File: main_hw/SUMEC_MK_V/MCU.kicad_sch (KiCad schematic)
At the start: 3 parts, among them U2 ESP32-S3-WROOM-1

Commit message: MK V Schematic update
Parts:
- added C34: 100n, Capacitor_SMD:C_0402_1005Metric, symbol Device:C
- added C35: 100nF, Capacitor_SMD:C_0805_2012Metric_Pad1.18x1.45mm_HandSolder, symbol Device:C
- added EEPROM1: 24CW1280T-I_OT, 24CW1280T-I_OT:SOT95P280X145-5N, symbol 24CW1280T-I_OT:24CW1280T-I_OT
- added U8: 24CW1280T-I/OT, Package_TO_SOT_SMD:SOT-23-5, symbol Memory_EEPROM:24AA02-OT
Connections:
- net +3V3: now also C34.1, C35.1, EEPROM1.4 (VCC), U8.4 (V_{CC})
- net GND: now also C34.2, C35.2, EEPROM1.2 (VSS), U8.2 (V_{SS})
- net SCL: now also U8.1 (SCL)
- net SDA: now also U8.3 (SDA)
- new net I2C1_SCL: EEPROM1.1 (SCL)
- new net I2C1_SDA: EEPROM1.3 (SDA)
- no-connect marks 5 -> 7
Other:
- note added: "CHANGE LABELS"
- note added: "EEPROM"
- note added: "I2C Addr.: 0x50"
- moved on the sheet: C20, C21, U2

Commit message: Schematic update - finalized
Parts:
- removed C34: 100n, Capacitor_SMD:C_0402_1005Metric, symbol Device:C
- removed EEPROM1: 24CW1280T-I_OT, 24CW1280T-I_OT:SOT95P280X145-5N, symbol 24CW1280T-I_OT:24CW1280T-I_OT
- removed U2: ESP32-S3-WROOM-1, PCM_Espressif:ESP32-S3-WROOM-1, symbol sumec_sch_lib:ESP32-S3-WROOM-1_CUSTOM_made_by_bismarx
- added U4: ESP32-S3-WROOM-1, PCM_Espressif:ESP32-S3-WROOM-1, symbol sumec_sch_lib:ESP32-S3-WROOM-1_CUSTOM_made_by_bismarx
- renumbered C35 to C20, C20 to C21, C21 to C22, U8 to U3
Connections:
- net +3V3: now also U4.2 (3V3)
- net BOOT: now also U4.27 (IO0)
- net EN: now also U4.3 (EN)
- net GND: now also U4.1 (GND), U4.40 (GND), U4.41 (GND)
- no-connect marks 7 -> 4
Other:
- note added: "I2C bus is pullled up internally by esp32"
- note removed: "FREE"
- title: SUMEC_MK_IV -> SUMEC_MK_V
- moved on the sheet: C20, U3

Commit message: MK V Schematic update
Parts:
- renumbered C20 to C24, C21 to C25, C22 to C26, U3 to U4, U4 to U5
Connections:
- net D-: now reaches U5.13 (IO19)
- net D+: now reaches U5.14 (IO20)
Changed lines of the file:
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@@
 		(at 208.28 96.52)
 	)
-	(bus_entry
-		(at 60.96 139.7)
-		(size 2.54 2.54)
-		(stroke
-			(width 0)
-			(type default)
-		)
-	)
 	(wire
 		(pts
@@
 	(wire
 		(pts
+			(xy 207.01 68.58) (xy 205.74 68.58)
+		)
+		(stroke
+			(width 0)
+			(type default)
+		)
+	)
+	(wire
+		(pts
 			(xy 186.69 40.64) (xy 186.69 46.99)
 		)
@@
 		(pts
 			(xy 93.98 135.89) (xy 93.98 139.7)
+		)
+		(stroke
+			(width 0)
+			(type default)
+		)
+	)
+	(wire
+		(pts
+			(xy 207.01 66.04) (xy 205.74 66.04)
 		)
 		(stroke
@@
 		)
 	)
+	(global_label "D+"
+		(shape input)
+		(at 207.01 68.58 0)
+		(fields_autoplaced yes)
+		(effects
+			(font
+				(face "Bahnschrift")
+				(size 1 1)
+				(color 0 0 0 1)
+			)
+			(justify left)
+		)
+		(property "Intersheetrefs" "${INTERSHEET_REFS}"
+			(at 210.8432 68.58 0)
+			(effects
+				(font
+					(size 1.27 1.27)
+				)
+				(justify left)
+				(hide yes)
+			)
+		)
+	)
 	(global_label "SCL"
 		(shape bidirectional)
@@
 		)
 	)
+	(global_label "D-"
+		(shape input)
+		(at 207.01 66.04 0)
+		(fields_autoplaced yes)
+		(effects
+			(font
+				(face "Bahnschrift")
+				(size 1 1)
+				(color 0 0 0 1)
+			)
+			(justify left)
+		)
+		(property "Intersheetrefs" "${INTERSHEET_REFS}"
+			(at 210.7748 66.04 0)
+			(effects
+				(font
+					(size 1.27 1.27)
+				)
+				(justify left)
+				(hide yes)
+			)
+		)
+	)
 	(symbol
 		(lib_name "GND_1")
@@
 		(on_board yes)
 		(dnp no)
-		(property "Reference" "#PWR050"
+		(property "Reference" "#PWR057"
 			(at 83.82 142.24 0)
 			(effects
@@
 			(project "SUMEC_MK_V"
 				(path "/900bd7ac-cdf9-4a2f-8b1f-2c21e3760046/7b93d7c5-db1a-415c-92e4-9ebec6cf195f"
-					(reference "#PWR050")
+					(reference "#PWR057")
 					(unit 1)
 				)
@@
 		(on_board yes)
 		(dnp no)
-		(property "Reference" "U4"
+		(property "Reference" "U5"
 			(at 162.56 104.775 0)
 			(effects
@@
 			(project ""
 				(path "/900bd7ac-cdf9-4a2f-8b1f-2c21e3760046/7b93d7c5-db1a-415c-92e4-9ebec6cf195f"
-					(reference "U4")
+					(reference "U5")
 					(unit 1)
 				)
@@
 		(dnp no)
 		(fields_autoplaced yes)
-		(property "Reference" "U3"
+		(property "Reference" "U4"
 			(at 96.1741 137.16 0)
 			(effects
@@
 			(project "SUMEC_MK_V"
 				(path "/900bd7ac-cdf9-4a2f-8b1f-2c21e3760046/7b93d7c5-db1a-415c-92e4-9ebec6cf195f"
-					(reference "U3")
+					(reference "U4")
 					(unit 1)
 				)
@@
 		(on_board yes)
 		(dnp no)
-		(property "Reference" "C20"
+		(property "Reference" "C24"
 			(at 86.106 130.302 90)
 			(effects
@@
 			(project "SUMEC_MK_V"
 				(path "/900bd7ac-cdf9-4a2f-8b1f-2c21e3760046/7b93d7c5-db1a-415c-92e4-9ebec6cf195f"
-					(reference "C20")
+					(reference "C24")
 					(unit 1)
 				)
@@
 		(dnp no)
 		(fields_autoplaced yes)
-		(property "Reference" "#PWR054"
+		(property "Reference" "#PWR061"
 			(at 186.69 113.03 0)
 			(effects
@@
 			(project "SUMEC_MK_V"
 				(path "/900bd7ac-cdf9-4a2f-8b1f-2c21e3760046/7b93d7c5-db1a-415c-92e4-9ebec6cf195f"
-					(reference "#PWR054")
+					(reference "#PWR061")
 					(unit 1)
 				)
@@
 		(on_board yes)
 		(dnp no)
-		(property "Reference" "C21"
+		(property "Reference" "C25"
 			(at 191.77 43.18 90)
 			(effects
@@
 			(project "SUMEC_MK_V"
 				(path "/900bd7ac-cdf9-4a2f-8b1f-2c21e3760046/7b93d7c5-db1a-415c-92e4-9ebec6cf195f"
-					(reference "C21")
+					(reference "C25")
 					(unit 1)
 				)
@@
 		(on_board yes)
 		(dnp no)
-		(property "Reference" "#PWR053"
+		(property "Reference" "#PWR060"
 			(at 186.69 41.91 0)
 			(effects
@@
 			(project "SUMEC_MK_V"
 				(path "/900bd7ac-cdf9-4a2f-8b1f-2c21e3760046/7b93d7c5-db1a-415c-92e4-9ebec6cf195f"
-					(reference "#PWR053")
+					(reference "#PWR060")
 					(unit 1)
 				)
@@
 		(on_board yes)
 		(dnp no)
-		(property "Reference" "#PWR052"
+		(property "Reference" "#PWR059"
 			(at 93.98 161.29 0)
 			(effects
@@
 			(project "SUMEC_MK_V"
 				(path "/900bd7ac-cdf9-4a2f-8b1f-2c21e3760046/7b93d7c5-db1a-415c-92e4-9ebec6cf195f"
-					(reference "#PWR052")
+					(reference "#PWR059")
 					(unit 1)
 				)
@@
 		(on_board yes)
 		(dnp no)
-		(property "Reference" "#PWR051"
+		(property "Reference" "#PWR058"
 			(at 93.98 137.16 0)
 			(effects
@@
 			(project "SUMEC_MK_V"
 				(path "/900bd7ac-cdf9-4a2f-8b1f-2c21e3760046/7b93d7c5-db1a-415c-92e4-9ebec6cf195f"
-					(reference "#PWR051")
+					(reference "#PWR058")
 					(unit 1)
 				)
@@
 		(dnp no)
 		(fields_autoplaced yes)
-		(property "Reference" "#PWR055"
+		(property "Reference" "#PWR062"
 			(at 201.93 54.61 0)
 			(effects
@@
 			(project "SUMEC_MK_V"
 				(path "/900bd7ac-cdf9-4a2f-8b1f-2c21e3760046/7b93d7c5-db1a-415c-92e4-9ebec6cf195f"
-					(reference "#PWR055")
+					(reference "#PWR062")
 					(unit 1)
 				)
@@
 		(on_board yes)
 		(dnp no)
-		(property "Reference" "C22"
+		(property "Reference" "C26"
 			(at 191.77 49.53 90)
 			(effects
@@
 			(project "SUMEC_MK_V"
 				(path "/900bd7ac-cdf9-4a2f-8b1f-2c21e3760046/7b93d7c5-db1a-415c-92e4-9ebec6cf195f"
-					(reference "C22")
+					(reference "C26")
 					(unit 1)
 				)

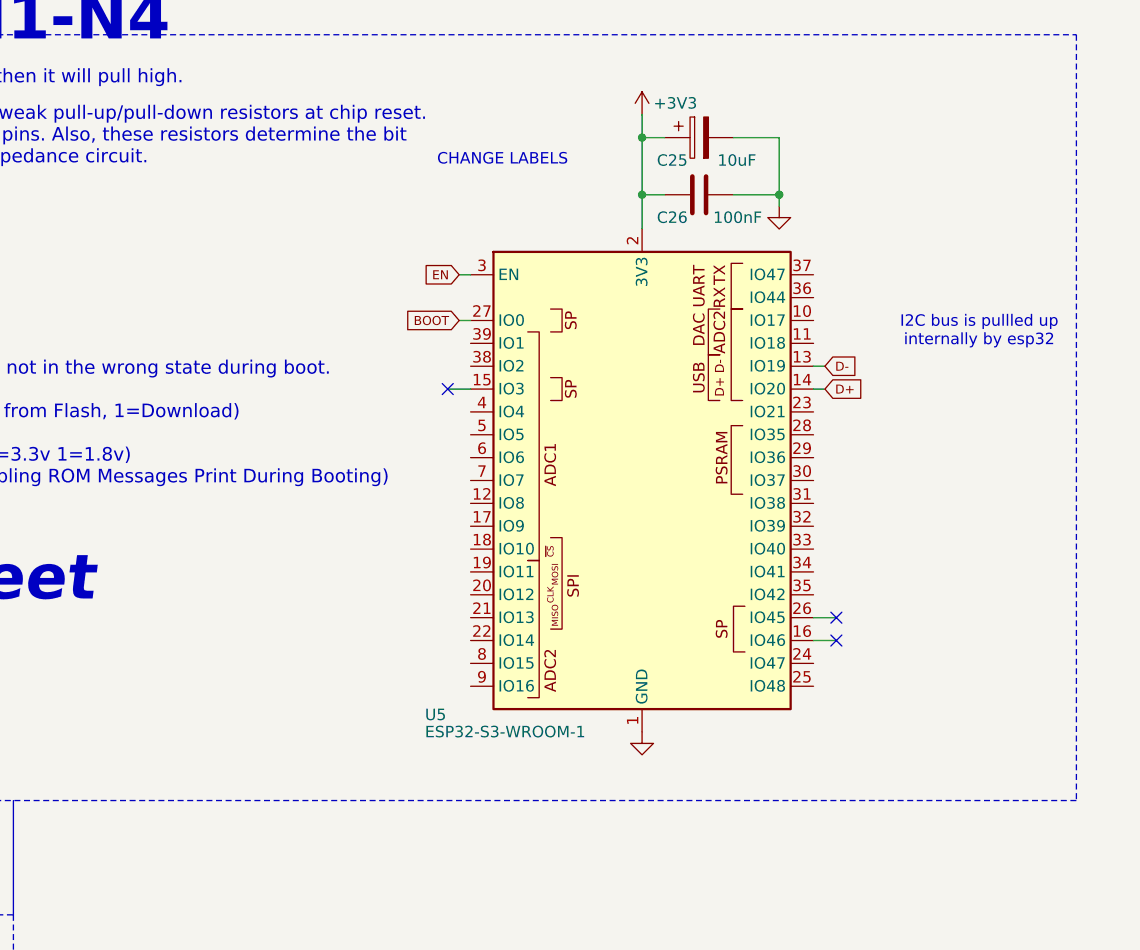
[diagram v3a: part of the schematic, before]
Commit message: PCB Update, signal routing
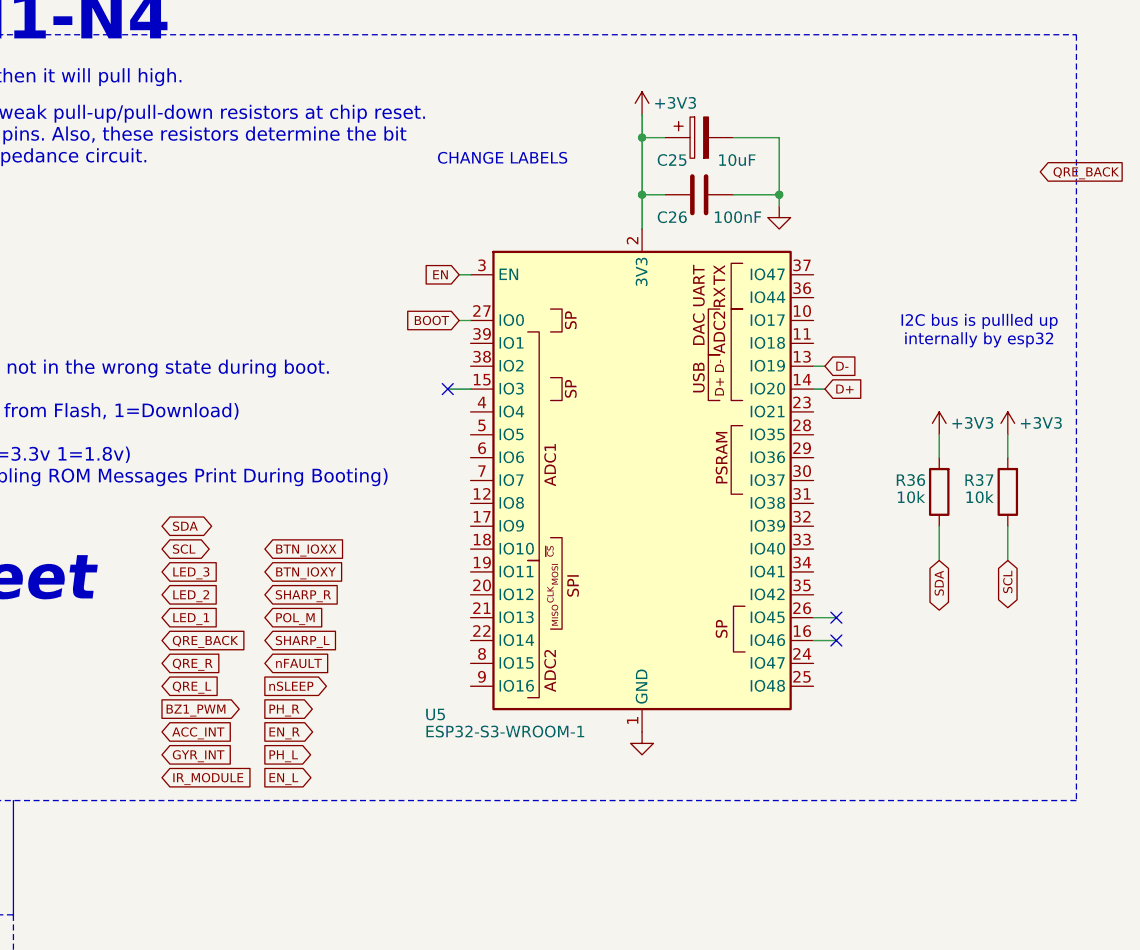
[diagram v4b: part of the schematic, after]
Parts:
- added R36, R37: 10k, Resistor_SMD:R_0805_2012Metric_Pad1.20x1.40mm_HandSolder, symbol Device:R
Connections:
- net +3V3: now also R36.2, R37.2
- net SCL: now also R37.1
- net SDA: now also R36.1

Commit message: a lot of routing and layout updates
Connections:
- net ACC_INT: now also U5.32 (IO39)
- net BTN_IOXX: now also U5.4 (IO4)
- net BTN_IOXY: now also U5.5 (IO5)
- net EN_L: now also U5.12 (IO8)
- net EN_R: now also U5.7 (IO7)
- net GYR_INT: now also U5.33 (IO40)
- net IR_MODULE: now also U5.34 (IO41)
- net LED_1: now also U5.37 (IO47)
- net LED_2: now also U5.38 (IO2)
- net LED_3: now also U5.39 (IO1)
- net PH_L: now also U5.11 (IO18)
- net POL_M: now also U5.19 (IO11)
- net QRE_BACK: now also U5.9 (IO16)
- net QRE_L: now also U5.22 (IO14)
- net QRE_R: now also U5.21 (IO13)
- net SCL: now also U5.35 (IO42)
- net SDA: now also U5.36 (IO44)
- net SHARP_L: now also U5.18 (IO10)
- net SHARP_R: now also U5.31 (IO38)
- net nFAULT: now also U5.8 (IO15)
- net nSLEEP: now also U5.10 (IO17)
- net VOLTAGE_ALERT: now reaches U5.17 (IO9)
- net POL_R: now reaches U5.20 (IO12)
- net PH_R_IO6: now reaches U5.6 (IO6)
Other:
- note added: "GPIO | NAME | DESC. 02 | MAIN_BTN | Schrack light switch; --debounced --pullup 05 | R_LED | LEDs, Indication --debug 06 | G_LED | LEDs, Indication --debug 09 | BUZZER | Passive buzzer 10 | MISO | SPI; SD Card 11 | CLOCK | SPI clock; SD Card, MAX7219 12 | MOSI | SPI; SD Card, MAX7219 04 | cSelect0 | Chipselect for MAX7219; --defHigh 13 | cSelect1 | Chipselect for SD Card; --defHigh 38 | D_EXT1 | E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"
- note added: "INPUT_PULLUP"

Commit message: routing update
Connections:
- net PH_R_IO6 renamed PH_R
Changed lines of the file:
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@@
 		)
 	)
-	(global_label "PH_R_IO6"
+	(global_label "PH_R"
 		(shape output)
 		(at 167.64 76.2 180)
@@
 		)
 		(property "Intersheetrefs" "${INTERSHEET_REFS}"
-			(at 159.5189 76.2 0)
+			(at 162.1352 76.2 0)
 			(effects
 				(font

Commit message: sumec pcb update
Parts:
- renumbered C24 to C21, C25 to C22, C26 to C23, R36 to R16, R37 to R17, U4 to U3, U5 to U4
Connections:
- net BZ_IO37: now reaches U4.30 (IO37)
- net LED_1 renamed LED_IO47
- net LED_2 renamed LED_IO02
- net LED_3 renamed LED_IO01
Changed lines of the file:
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@@
 		)
 	)
-	(global_label "LED_3"
+	(global_label "LED_IO01"
 		(shape input)
 		(at 167.64 63.5 180)
@@
 		)
 		(property "Intersheetrefs" "${INTERSHEET_REFS}"
-			(at 161.5588 63.5 0)
+			(at 159.8003 63.5 0)
 			(effects
 				(font
@@
 		)
 	)
-	(global_label "BZ1_PWM"
+	(global_label "BZ_IO37"
 		(shape output)
-		(at 208.28 72.39 0)
+		(at 205.74 78.74 0)
 		(fields_autoplaced yes)
 		(effects
@@
 		)
 		(property "Intersheetrefs" "${INTERSHEET_REFS}"
-			(at 216.3483 72.39 0)
+			(at 212.9154 78.74 0)
 			(effects
 				(font
@@
 		)
 	)
-	(global_label "LED_1"
+	(global_label "LED_IO47"
 		(shape input)
 		(at 205.74 55.88 0)
@@
 		)
 		(property "Intersheetrefs" "${INTERSHEET_REFS}"
-			(at 211.5467 55.88 0)
+			(at 213.8709 55.88 0)
 			(effects
 				(font
@@
 		)
 	)
-	(global_label "LED_2"
+	(global_label "LED_IO02"
 		(shape input)
 		(at 167.64 66.04 180)
@@
 		)
 		(property "Intersheetrefs" "${INTERSHEET_REFS}"
-			(at 161.5754 66.04 0)
+			(at 159.5423 66.04 0)
 			(effects
 				(font
@@
 		(on_board yes)
 		(dnp no)
-		(property "Reference" "#PWR057"
+		(property "Reference" "#PWR052"
 			(at 83.82 142.24 0)
 			(effects
@@
 			(project "SUMEC_MK_V"
 				(path "/900bd7ac-cdf9-4a2f-8b1f-2c21e3760046/7b93d7c5-db1a-415c-92e4-9ebec6cf195f"
-					(reference "#PWR057")
+					(reference "#PWR052")
 					(unit 1)
 				)
@@
 		(on_board yes)
 		(dnp no)
-		(property "Reference" "U5"
+		(property "Reference" "U4"
 			(at 162.56 104.775 0)
 			(effects
@@
 			(project ""
 				(path "/900bd7ac-cdf9-4a2f-8b1f-2c21e3760046/7b93d7c5-db1a-415c-92e4-9ebec6cf195f"
-					(reference "U5")
+					(reference "U4")
 					(unit 1)
 				)
@@
 		(dnp no)
 		(fields_autoplaced yes)
-		(property "Reference" "U4"
+		(property "Reference" "U3"
 			(at 96.1741 137.16 0)
 			(effects
@@
 			(project "SUMEC_MK_V"
 				(path "/900bd7ac-cdf9-4a2f-8b1f-2c21e3760046/7b93d7c5-db1a-415c-92e4-9ebec6cf195f"
-					(reference "U4")
+					(reference "U3")
 					(unit 1)
 				)
@@
 		(on_board yes)
 		(dnp no)
-		(property "Reference" "#PWR0112"
+		(property "Reference" "#PWR059"
 			(at 227.33 77.47 0)
 			(effects
@@
 			(project "SUMEC_MK_V"
 				(path "/900bd7ac-cdf9-4a2f-8b1f-2c21e3760046/7b93d7c5-db1a-415c-92e4-9ebec6cf195f"
-					(reference "#PWR0112")
+					(reference "#PWR059")
 					(unit 1)
 				)
@@
 		(on_board yes)
 		(dnp no)
-		(property "Reference" "#PWR0105"
+		(property "Reference" "#PWR058"
 			(at 219.71 77.47 0)
 			(effects
@@
 			(project "SUMEC_MK_V"
 				(path "/900bd7ac-cdf9-4a2f-8b1f-2c21e3760046/7b93d7c5-db1a-415c-92e4-9ebec6cf195f"
-					(reference "#PWR0105")
+					(reference "#PWR058")
 					(unit 1)
 				)
@@
 		(on_board yes)
 		(dnp no)
-		(property "Reference" "R36"
+		(property "Reference" "R16"
 			(at 216.535 78.74 0)
 			(effects
@@
 			(project "SUMEC_MK_V"
 				(path "/900bd7ac-cdf9-4a2f-8b1f-2c21e3760046/7b93d7c5-db1a-415c-92e4-9ebec6cf195f"
-					(reference "R36")
+					(reference "R16")
 					(unit 1)
 				)
@@
 		(on_board yes)
 		(dnp no)
-		(property "Reference" "C24"
+		(property "Reference" "C21"
 			(at 86.106 130.302 90)
 			(effects
@@
 			(project "SUMEC_MK_V"
 				(path "/900bd7ac-cdf9-4a2f-8b1f-2c21e3760046/7b93d7c5-db1a-415c-92e4-9ebec6cf195f"
-					(reference "C24")
+					(reference "C21")
 					(unit 1)
 				)
@@
 		(dnp no)
 		(fields_autoplaced yes)
-		(property "Reference" "#PWR061"
+		(property "Reference" "#PWR056"
 			(at 186.69 113.03 0)
 			(effects
@@
 			(project "SUMEC_MK_V"
 				(path "/900bd7ac-cdf9-4a2f-8b1f-2c21e3760046/7b93d7c5-db1a-415c-92e4-9ebec6cf195f"
-					(reference "#PWR061")
+					(reference "#PWR056")
 					(unit 1)
 				)
@@
 		(on_board yes)
 		(dnp no)
-		(property "Reference" "C25"
+		(property "Reference" "C22"
 			(at 191.77 43.18 90)
 			(effects
@@
 			(project "SUMEC_MK_V"
 				(path "/900bd7ac-cdf9-4a2f-8b1f-2c21e3760046/7b93d7c5-db1a-415c-92e4-9ebec6cf195f"
-					(reference "C25")
+					(reference "C22")
 					(unit 1)
 				)
@@
 		(on_board yes)
 		(dnp no)
-		(property "Reference" "#PWR060"
+		(property "Reference" "#PWR055"
 			(at 186.69 41.91 0)
 			(effects
@@
 			(project "SUMEC_MK_V"
 				(path "/900bd7ac-cdf9-4a2f-8b1f-2c21e3760046/7b93d7c5-db1a-415c-92e4-9ebec6cf195f"
-					(reference "#PWR060")
+					(reference "#PWR055")
 					(unit 1)
 				)
@@
 		(on_board yes)
 		(dnp no)
-		(property "Reference" "R37"
+		(property "Reference" "R17"
 			(at 224.155 78.74 0)
 			(effects
@@
 			(project "SUMEC_MK_V"
 				(path "/900bd7ac-cdf9-4a2f-8b1f-2c21e3760046/7b93d7c5-db1a-415c-92e4-9ebec6cf195f"
-					(reference "R37")
+					(reference "R17")
 					(unit 1)
 				)
@@
 		(on_board yes)
 		(dnp no)
-		(property "Reference" "#PWR059"
+		(property "Reference" "#PWR054"
 			(at 93.98 161.29 0)
 			(effects
@@
 			(project "SUMEC_MK_V"
 				(path "/900bd7ac-cdf9-4a2f-8b1f-2c21e3760046/7b93d7c5-db1a-415c-92e4-9ebec6cf195f"
-					(reference "#PWR059")
+					(reference "#PWR054")
 					(unit 1)
 				)
@@
 		(on_board yes)
 		(dnp no)
-		(property "Reference" "#PWR058"
+		(property "Reference" "#PWR053"
 			(at 93.98 137.16 0)
 			(effects
@@
 			(project "SUMEC_MK_V"
 				(path "/900bd7ac-cdf9-4a2f-8b1f-2c21e3760046/7b93d7c5-db1a-415c-92e4-9ebec6cf195f"
-					(reference "#PWR058")
+					(reference "#PWR053")
 					(unit 1)
 				)
@@
 		(dnp no)
 		(fields_autoplaced yes)
-		(property "Reference" "#PWR062"
+		(property "Reference" "#PWR057"
 			(at 201.93 54.61 0)
 			(effects
@@
 			(project "SUMEC_MK_V"
 				(path "/900bd7ac-cdf9-4a2f-8b1f-2c21e3760046/7b93d7c5-db1a-415c-92e4-9ebec6cf195f"
-					(reference "#PWR062")
+					(reference "#PWR057")
 					(unit 1)
 				)
@@
 		(on_board yes)
 		(dnp no)
-		(property "Reference" "C26"
+		(property "Reference" "C23"
 			(at 191.77 49.53 90)
 			(effects
@@
 			(project "SUMEC_MK_V"
 				(path "/900bd7ac-cdf9-4a2f-8b1f-2c21e3760046/7b93d7c5-db1a-415c-92e4-9ebec6cf195f"
-					(reference "C26")
+					(reference "C23")
 					(unit 1)
 				)

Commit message: new qre board
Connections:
- net BZ_IO37 is gone; now on net IR_MODULE: U4.30 (IO37)
- net IR_MODULE: no longer U4.34 (IO41)
- net SCL: now also U4.34 (IO41); no longer U4.35 (IO42)
- net SDA: now also U4.35 (IO42); no longer U4.36 (IO44)
- net LED_IO36: now reaches U4.29 (IO36)
- net BTN_IOXX renamed BTN_IO04
- net BTN_IOXY renamed BTN_IO05
- net LED_IO02 renamed BZ_PWM
- new net LED_IO44: U4.36 (IO44)
- no-connect marks 4 -> 8
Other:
- note removed: "I2C bus is pullled up internally by esp32"
- moved on the sheet: R16, R17
